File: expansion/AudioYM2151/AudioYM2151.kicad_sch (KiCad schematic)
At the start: 17 parts, among them J1 JTAG, J2 D68K_64PIN_BOARD, Q1 2N4403, U1 XC95144XL-TQ100, U2 74LS125

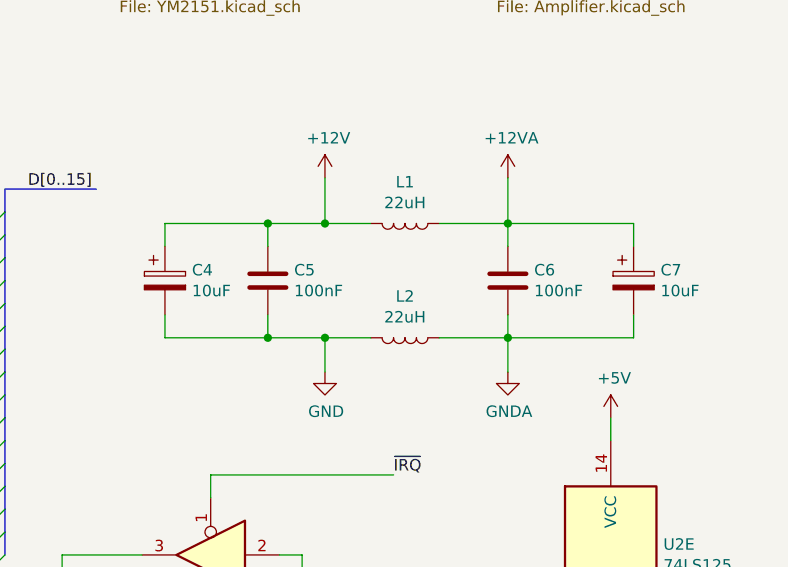
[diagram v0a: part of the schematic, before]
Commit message: All projects updated to KiCAD 7 format files
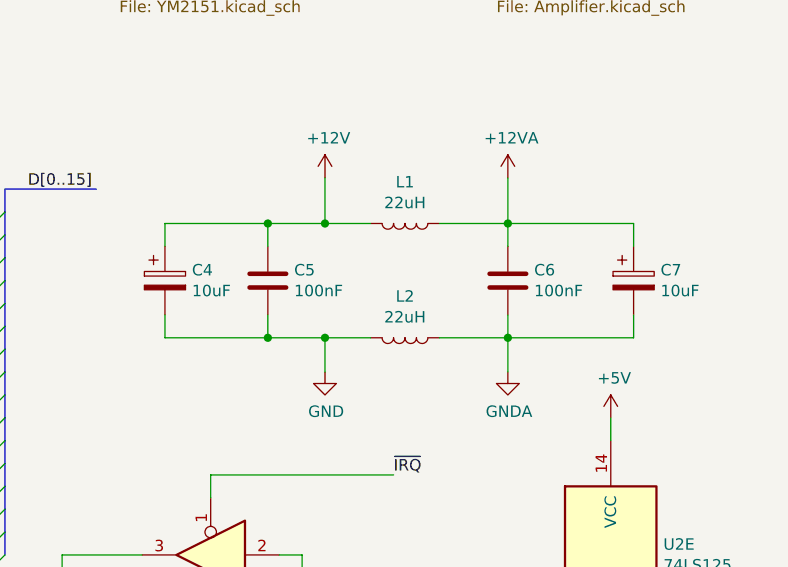
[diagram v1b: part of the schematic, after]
